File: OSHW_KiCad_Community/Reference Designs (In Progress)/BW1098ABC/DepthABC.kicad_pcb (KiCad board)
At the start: 4 copper layers, 150 x 65.2 mm, 118 parts, among them J1 Conn_02x05_Odd_Even, J13 DF23C-50DP-0.5V_92_, J2 FAN, J3 BW1099EMB_SoM, J4 Conn_02x05_Odd_Even, J5 USBC 3.1 Vertical, J6 26_pin_FFC, J7 26_pin_FFC, J9 26_pin_FFC, Q1 RK7002B, Q2 RK7002B, Q3 RK7002B, Q4 RK7002B, Q5 RK7002B, U1 2-bit bidirectional level shi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, U6 USB Type-C Switch, U7 USB Type-C Port Control

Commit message: abc updates
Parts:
- moved FID5 30.3 mm to (156.0, 100.6)
- moved FID1 2.76 mm to (184.7, 119.8)
- moved R40 0.73 mm to (234.6, 102.0)
- moved Q1 0.31 mm to (136.0, 110.1)
- moved R38 0.23 mm to (229.9, 106.1)
- moved FID4 0.05 mm to (260.2, 130.7)
- renumbered R28 to R11, R32 to R12, R14 to R13, R5 to R14, R6 to R15, R7 to R27, R38 to R28, R11 to R31, R39 to R32, R12 to R33, R40 to R34, R13 to R37, R41 to R38, R42 to R39, R43 to R40, R44 to R41, R31 to R5, R15 to R6, R27 to R7
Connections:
- net Earth renamed GND
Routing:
- net SD_HST0_D3: track 93.6 -> 96.9 mm
- net Net-(R11-Pad2): track 5.35 -> 3.41 mm
- net I2C2_SDA: track 126.1 -> 125.0 mm
- net Net-(Q1-Pad2): track 3.80 -> 2.72 mm, vias 1 -> 0
- net MIPI_RX4_D1_N: track 70.4 -> 69.5 mm
- net MIPI_RX5_D2_N: track 75.9 -> 75.0 mm
- net MIPI_RX4_D1_P: track 70.6 -> 69.9 mm
- net MIPI_RX5_D2_P: track 76.1 -> 75.3 mm
- net /USBC&POWER/P0.04: track 36.4 -> 37.1 mm
- net _RST: track 156.3 -> 155.8 mm
- net GND: track 284.2 -> 284.5 mm, vias 71 -> 103

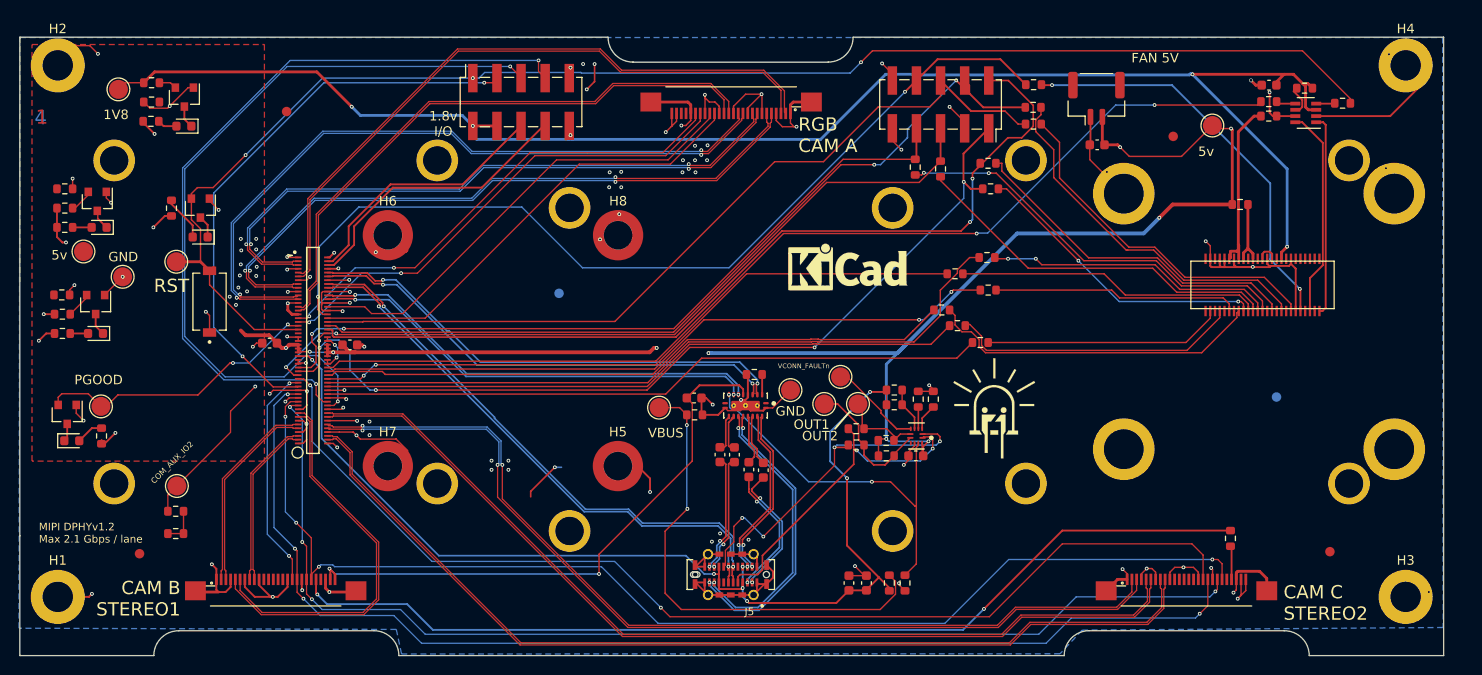
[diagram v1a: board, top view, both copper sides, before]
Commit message: depthabc skew matching
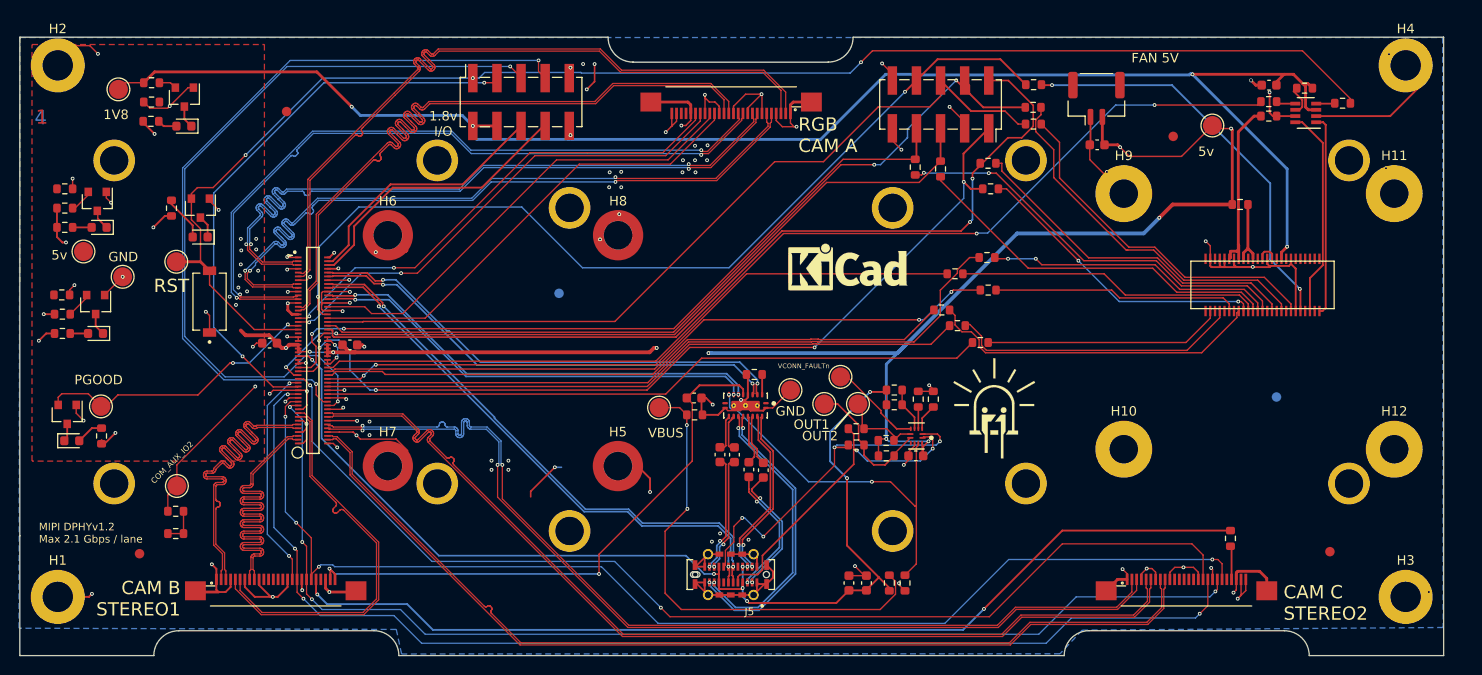
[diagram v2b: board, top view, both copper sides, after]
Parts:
- H10, H11, H12, H9: footprint ABC:4881 -> MountingHole:MountingHole_3mm_Pad
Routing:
- net MIPI_RX2_C_N: track 17.9 -> 41.3 mm
- net MIPI_RX2_C_P: track 17.5 -> 41.0 mm
- net MIPI_RX2_D0_P: track 20.6 -> 41.6 mm
- net MIPI_RX2_D0_N: track 21.0 -> 41.4 mm
- net MIPI_RX5_D3_P: track 61.7 -> 75.9 mm
- net MIPI_RX5_D3_N: track 62.2 -> 75.8 mm
- net MIPI_RX4_C_N: track 67.1 -> 76.0 mm
- net MIPI_RX4_C_P: track 67.4 -> 75.8 mm
- net MIPI_RX4_D0_P: track 69.2 -> 75.9 mm
- net MIPI_RX4_D1_N: track 69.5 -> 76.0 mm
- net MIPI_RX4_D1_P: track 69.9 -> 76.0 mm
- net MIPI_RX4_D0_N: track 69.7 -> 75.8 mm
- net MIPI_RX3_D1_N: track 99.9 -> 103.4 mm
- net MIPI_RX3_D0_N: track 99.9 -> 103.3 mm
- net MIPI_RX3_D1_P: track 100.2 -> 103.2 mm
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
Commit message: skew
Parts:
- moved TP2 5.26 mm to (131.9, 119.9)
- moved R34 3.74 mm to (132.1, 112.5)
- moved D1 3.74 mm to (135.7, 116.5)
- moved Q1 3.74 mm to (135.5, 113.8)
- moved R1 3.74 mm to (132.1, 114.5)
- moved R2 3.74 mm to (132.1, 116.5)
- moved TP10 3.04 mm to (136.3, 120.0)
- moved Q4 2.77 mm to (136.2, 123.7)
- moved R30 2.77 mm to (132.7, 126.8)
- moved R33 2.77 mm to (132.6, 122.7)
- moved D4 2.77 mm to (136.2, 126.8)
- moved R29 2.77 mm to (132.7, 124.7)
- moved H10 2.00 mm to (246.2, 136.2)
- moved H11 2.00 mm to (274.7, 109.3)
- moved H12 2.00 mm to (274.7, 136.2)
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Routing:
- net USB_D_N: track 58.6 -> 85.0 mm
- net USB_D_P: track 59.0 -> 85.0 mm
- net /USBC&POWER/RXB_P: track 18.3 -> 31.4 mm
- net /USBC&POWER/RXB_N: track 18.3 -> 31.1 mm
- net /USBC&POWER/TXC_N: track 12.3 -> 21.1 mm
- net /USBC&POWER/TXC_P: track 12.3 -> 21.1 mm
- net /USBC&POWER/TXB_N: track 13.9 -> 21.1 mm
- net /USBC&POWER/TXB_P: track 14.4 -> 21.1 mm
- net GND: track 281.5 -> 287.8 mm, vias 102 -> 100
- net (no net): track 4.86 -> 0.00 mm, vias 1 -> 0
- net USB_TX_N: track 47.6 -> 52.2 mm
- net /USBC&POWER/P0.11: track 36.2 -> 40.4 mm
- net USB_TX_P: track 48.3 -> 52.1 mm
- net /USBC&POWER/P0.08: track 38.7 -> 41.6 mm
- net /USBC&POWER/P0.04: track 37.1 -> 40.0 mm
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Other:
- board size 150 x 65.2 mm -> 152 x 65.2 mm
